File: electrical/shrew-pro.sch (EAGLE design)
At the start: 52 parts, among them IC1 LMR16006YQ3DDCTQ1, U1 ESP32-PICO-D4, U2 SX1280IMLTRT, U3 DRV8244SQRYJRQ1, U4 DRV8244SQRYJRQ1, X1 PIN-1X-BIG, X2 PIN-1X-BIG, X3 PIN-1X-BIG, X4 PIN-1X-BIG, X5 PIN-1X-BIG, X6 PIN-1X-BIG, Y1 52MHz TCXO

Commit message: placed a PCBA order for shrew-lite
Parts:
- C14, C15: value (none) -> 100n
- C16, C18, C19, C20, C21, C22, C23: value (none) -> 10u
- R4: value (none) -> 68K
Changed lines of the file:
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@@
 <part name="X3" library="shrew-core" deviceset="PIN-1X" device="-BIG"/>
 <part name="X4" library="shrew-core" deviceset="PIN-1X" device="-BIG"/>
-<part name="C14" library="shrew-common" deviceset="CAP" device="0402-CAP"/>
-<part name="C15" library="shrew-common" deviceset="CAP" device="0402-CAP"/>
+<part name="C14" library="shrew-common" deviceset="CAP" device="0402-CAP" value="100n"/>
+<part name="C15" library="shrew-common" deviceset="CAP" device="0402-CAP" value="100n"/>
 <part name="X5" library="shrew-core" deviceset="PIN-1X" device="-BIG" value="PIN-1X-BIG"/>
 <part name="P+11" library="shrew-common" deviceset="+24V" device=""/>
 <part name="X6" library="shrew-core" deviceset="PIN-1X" device="-BIG" value="PIN-1X-BIG"/>
 <part name="GND24" library="shrew-common" deviceset="GND" device=""/>
-<part name="C16" library="shrew-common" deviceset="CAP" device="0805"/>
-<part name="C18" library="shrew-common" deviceset="CAP" device="0805"/>
-<part name="C19" library="shrew-common" deviceset="CAP" device="0805"/>
+<part name="C16" library="shrew-common" deviceset="CAP" device="0805" value="10u"/>
+<part name="C18" library="shrew-common" deviceset="CAP" device="0805" value="10u"/>
+<part name="C19" library="shrew-common" deviceset="CAP" device="0805" value="10u"/>
 <part name="P+14" library="shrew-common" deviceset="+24V" device=""/>
 <part name="GND25" library="shrew-common" deviceset="GND" device=""/>
-<part name="C20" library="shrew-common" deviceset="CAP" device="0805"/>
+<part name="C20" library="shrew-common" deviceset="CAP" device="0805" value="10u"/>
 <part name="C25" library="shrew-common" deviceset="CAP" device="0805" value="10u"/>
 <part name="GND23" library="shrew-common" deviceset="GND" device=""/>
-<part name="R4" library="shrew-common" deviceset="RESISTOR" device="0402-REV"/>
+<part name="R4" library="shrew-common" deviceset="RESISTOR" device="0402-REV" value="68K"/>
 <part name="P+10" library="shrew-common" deviceset="+24V" device=""/>
 <part name="U3" library="shrew-core" deviceset="DRV8244SQRYJRQ1" device=""/>
@@
 <part name="GND29" library="shrew-common" deviceset="GND" device=""/>
 <part name="GND30" library="shrew-common" deviceset="GND" device=""/>
-<part name="C21" library="shrew-common" deviceset="CAP" device="0805"/>
-<part name="C22" library="shrew-common" deviceset="CAP" device="0805"/>
-<part name="C23" library="shrew-common" deviceset="CAP" device="0805"/>
+<part name="C21" library="shrew-common" deviceset="CAP" device="0805" value="10u"/>
+<part name="C22" library="shrew-common" deviceset="CAP" device="0805" value="10u"/>
+<part name="C23" library="shrew-common" deviceset="CAP" device="0805" value="10u"/>
 <part name="P+17" library="shrew-common" deviceset="3.3V" device=""/>
 <part name="C24" library="shrew-common" deviceset="CAP" device="0805" value="10u"/>
@@
 <instance part="X6" gate="G$1" x="429.26" y="124.46"/>
 <instance part="GND24" gate="1" x="421.64" y="119.38"/>
-<instance part="C16" gate="G$1" x="421.64" y="86.36"/>
-<instance part="C18" gate="G$1" x="431.8" y="86.36"/>
-<instance part="C19" gate="G$1" x="441.96" y="86.36"/>
+<instance part="C16" gate="G$1" x="421.64" y="86.36" smashed="yes">
+<attribute name="NAME" x="423.164" y="89.281" size="1.778" layer="95"/>
+</instance>
+<instance part="C18" gate="G$1" x="431.8" y="86.36" smashed="yes">
+<attribute name="NAME" x="433.324" y="89.281" size="1.778" layer="95"/>
+</instance>
+<instance part="C19" gate="G$1" x="441.96" y="86.36" smashed="yes">
+<attribute name="NAME" x="443.484" y="89.281" size="1.778" layer="95"/>
+</instance>
 <instance part="P+14" gate="1" x="421.64" y="99.06"/>
 <instance part="GND25" gate="1" x="421.64" y="76.2"/>
-<instance part="C20" gate="G$1" x="452.12" y="86.36"/>
+<instance part="C20" gate="G$1" x="452.12" y="86.36" smashed="yes">
+<attribute name="NAME" x="453.644" y="89.281" size="1.778" layer="95"/>
+</instance>
 <instance part="C25" gate="G$1" x="393.7" y="149.86"/>
 <instance part="GND23" gate="1" x="474.98" y="114.3"/>
@@
 <instance part="GND29" gate="1" x="431.8" y="-43.18"/>
 <instance part="GND30" gate="1" x="431.8" y="15.24"/>
-<instance part="C21" gate="G$1" x="462.28" y="86.36"/>
-<instance part="C22" gate="G$1" x="472.44" y="86.36"/>
-<instance part="C23" gate="G$1" x="482.6" y="86.36"/>
+<instance part="C21" gate="G$1" x="462.28" y="86.36" smashed="yes">
+<attribute name="NAME" x="463.804" y="89.281" size="1.778" layer="95"/>
+</instance>
+<instance part="C22" gate="G$1" x="472.44" y="86.36" smashed="yes">
+<attribute name="NAME" x="473.964" y="89.281" size="1.778" layer="95"/>
+</instance>
+<instance part="C23" gate="G$1" x="482.6" y="86.36" smashed="yes">
+<attribute name="NAME" x="484.124" y="89.281" size="1.778" layer="95"/>
+</instance>
 <instance part="P+17" gate="G$1" x="474.98" y="132.08"/>
 <instance part="C24" gate="G$1" x="510.54" y="91.44"/>

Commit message: wip
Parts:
- added TP1, TP2, TP3: M01-1.0MM-TP, shrew-common:M01-1.0MM-TP
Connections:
- net RADIO-RST: now also TP3.1
- net SIG1: now also TP1.1
- net SIG2: now also TP2.1
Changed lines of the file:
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@@
 <part name="P+8" library="shrew-common" deviceset="+24V" device=""/>
 <part name="C27" library="shrew-common" deviceset="CAP" device="0805" value="10u"/>
+<part name="TP1" library="shrew-common" deviceset="M01" device="-1.0MM-TP" value=""/>
+<part name="TP2" library="shrew-common" deviceset="M01" device="-1.0MM-TP" value=""/>
+<part name="TP3" library="shrew-common" deviceset="M01" device="-1.0MM-TP" value=""/>
 </parts>
 <sheets>
@@
 <instance part="P+8" gate="1" x="322.58" y="172.72"/>
 <instance part="C27" gate="G$1" x="474.98" y="124.46"/>
+<instance part="TP1" gate="G$1" x="386.08" y="-20.32"/>
+<instance part="TP2" gate="G$1" x="386.08" y="-33.02"/>
+<instance part="TP3" gate="G$1" x="386.08" y="-48.26"/>
 </instances>
 <busses>
@@
 <label x="431.8" y="-15.24" size="1.27" layer="95" rot="R180" xref="yes"/>
 </segment>
+<segment>
+<pinref part="TP3" gate="G$1" pin="1"/>
+<wire x1="393.7" y1="-48.26" x2="396.24" y2="-48.26" width="0.1524" layer="91"/>
+<label x="396.24" y="-48.26" size="1.27" layer="95" xref="yes"/>
+</segment>
 </net>
 <net name="RADIO-BUSY" class="0">
@@
 <label x="431.8" y="-25.4" size="1.27" layer="95" rot="R180" xref="yes"/>
 </segment>
+<segment>
+<pinref part="TP2" gate="G$1" pin="1"/>
+<wire x1="393.7" y1="-33.02" x2="396.24" y2="-33.02" width="0.1524" layer="91"/>
+<label x="396.24" y="-33.02" size="1.27" layer="95" xref="yes"/>
+</segment>
 </net>
 <net name="SIG1" class="0">
@@
 <label x="431.8" y="-20.32" size="1.27" layer="95" rot="R180" xref="yes"/>
 </segment>
-</net>
+<segment>
+<pinref part="TP1" gate="G$1" pin="1"/>
+<wire x1="393.7" y1="-20.32" x2="396.24" y2="-20.32" width="0.1524" layer="91"/>
+<label x="396.24" y="-20.32" size="1.27" layer="95" xref="yes"/>
+</segment>
+</net>

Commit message: sorted component ref des
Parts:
- removed FL1: 2450FM07D0034T, shrew-core:2450FM07D0034T
- added Y2: 52MHz TCXO, shrew-common:OSCILLATOR-TG2016SMN
- C1: value 1n -> 100n
- C10, C5, C6, C7, C8, C9: value 100n -> 10u; device shrew-common:CAP0402-REV -> shrew-common:CAP0805
- C11: value 10uF 25V -> 10u
- C12: value DNP -> 100n; device shrew-common:CAP0402-CAP -> shrew-common:CAP0402-REV
- C13: value 470n -> 100n
- C14: device shrew-common:CAP0402-CAP -> shrew-common:CAP0402-REV
- C15: value 100n -> 10uF 25V; device shrew-common:CAP0402-CAP -> shrew-common:CAP0805
- C16, C18, C25: value 10u -> 470n; device shrew-common:CAP0805 -> shrew-common:CAP0402-REV
- C17: value 470n -> DNP; device shrew-common:CAP0402-REV -> shrew-common:CAP0402-CAP
- C19, C20: value 10u -> 10n; device shrew-common:CAP0805 -> shrew-common:CAP0402-REV
- C2: value 470n -> 10u; device shrew-common:CAP0402-REV -> shrew-common:CAP0805
- C21: value 10u -> 1n; device shrew-common:CAP0805 -> shrew-common:CAP0402-REV
- C22, C23, C24: value 10u -> 100n; device shrew-common:CAP0805 -> shrew-common:CAP0402-REV
- C26: device shrew-common:CAP0402-REV -> shrew-common:CAP0402-CAP
- C27: value 10u -> 100n; device shrew-common:CAP0805 -> shrew-common:CAP0402-CAP
- C3, C4: value 10n -> 10u; device shrew-common:CAP0402-REV -> shrew-common:CAP0805
- D1: value 3V6 -> (none); device shrew-common:DIODE-ZENER-BZT52 -> shrew-common:DIODESOD
- D2: value (none) -> 3V6; device shrew-common:DIODESOD -> shrew-common:DIODE-ZENER-BZT52
- L1: value 15u -> 6u8
- L2: value 6u8 -> 15u
- R2: value 10K -> 68K
- R4: value 68K -> 10K
- U3, U4: value DRV8244SQRYJRQ1 -> DRV8244HQRYJRQ1
- Y1: value 52MHz TCXO -> 2450FM07D0034T; device shrew-common:OSCILLATOR-TG2016SMN -> shrew-core:2450FM07D0034T
- renumbered EDGE1 to JP1
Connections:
- net +24V: now also C10.1, C11.1, C3.1, C5.1, C6.1, C7.1, C8.1, C9.1, R2.2, X1.P$1; no longer C16.1, C18.1, C19.1, C20.1, C21.1, C22.1, C23.1, C24.1, R4.2, X5.P$1
- net 3.3V: now also C12.1, C13.1, C14.1, C15.1, C2.1, C22.2, C23.2, C24.2, C4.1, L1.2, Y2.VCC; no longer C10.1, C11.1, C25.1, C27.1, C5.2, C6.2, C7.2, C8.1, C9.1, L2.2, Y1.VCC
- net BATT-ADC: now also C18.1, D2.C, R4.2; no longer C17.1, D1.C, R2.2
- net ESP-BOOT: now also C17.2; no longer C12.2
- net ESP-EN: now also C16.2; no longer C13.2
- net GND: now also C12.2, C13.2, C14.2, C15.2, C16.1, C17.1, C19.1, C2.2, C20.1, C22.1, C23.1, C24.1, C25.1, C3.2, C4.2, C5.2, C6.2, C7.2, R4.1, X2.P$1, Y2.GND; no longer C12.1, C13.1, C16.2, C17.2, C19.2, C2.1, C20.2, C21.2, C22.2, C23.2, C24.2, C25.2, C27.2, C3.1, C4.1, C5.1, C6.1, C7.1, R2.1, X6.P$1, Y1.GND
- net MOTOR1: now also C26.1, X3.P$1; no longer C14.1, X2.P$1
- net MOTOR2: now also C26.2, X4.P$1; no longer C14.2, X1.P$1
- net MOTOR3: now also C27.1, X5.P$1; no longer C15.1, X4.P$1
- net MOTOR4: now also C27.2, X6.P$1; no longer C15.2, X3.P$1
- net N$10: now also C1.1, D1.C, L1.1; no longer C26.1, D2.C, L2.1
- net N$11: now also C20.2; no longer C3.2
- net N$2: now also C21.1, Y2.OUT; no longer C1.1, Y1.OUT
- net N$3: now also C21.2; no longer C1.2
- net N$4: now also C1.2; no longer C26.2
- net N$6: now also Y1.IN; no longer FL1.IN
- net N$7: now also Y1.OUT; no longer FL1.OUT
- net N$9: now also L2.2; no longer L1.2
- net RADIO-VDD: now also C19.2, C25.2, L2.1; no longer C2.2, C4.2, L1.1
- net V-ADC: now also R2.1; no longer R4.1
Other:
- moved on the sheet: ANT2, C1, C10, C11, C12, C13, C14, C15, C16, C17, C18, C19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

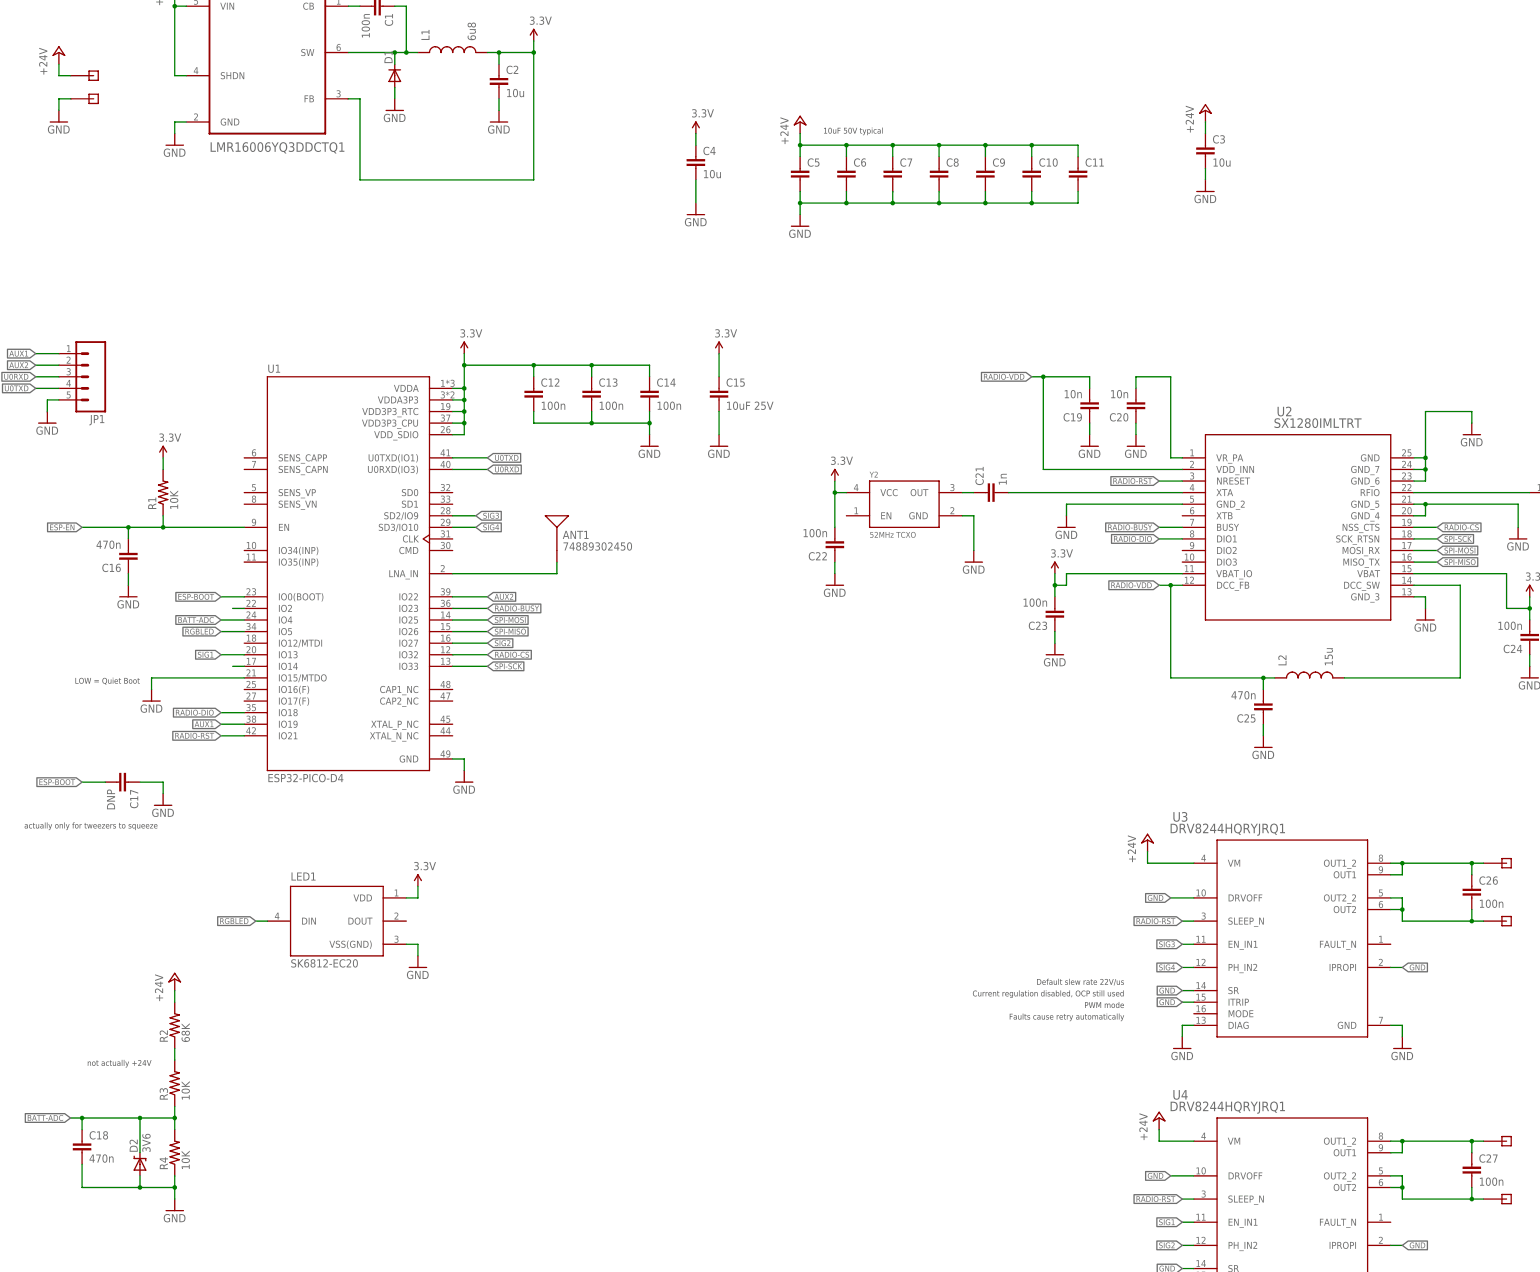
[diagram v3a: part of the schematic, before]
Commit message: shrew-pro with additional capacitors
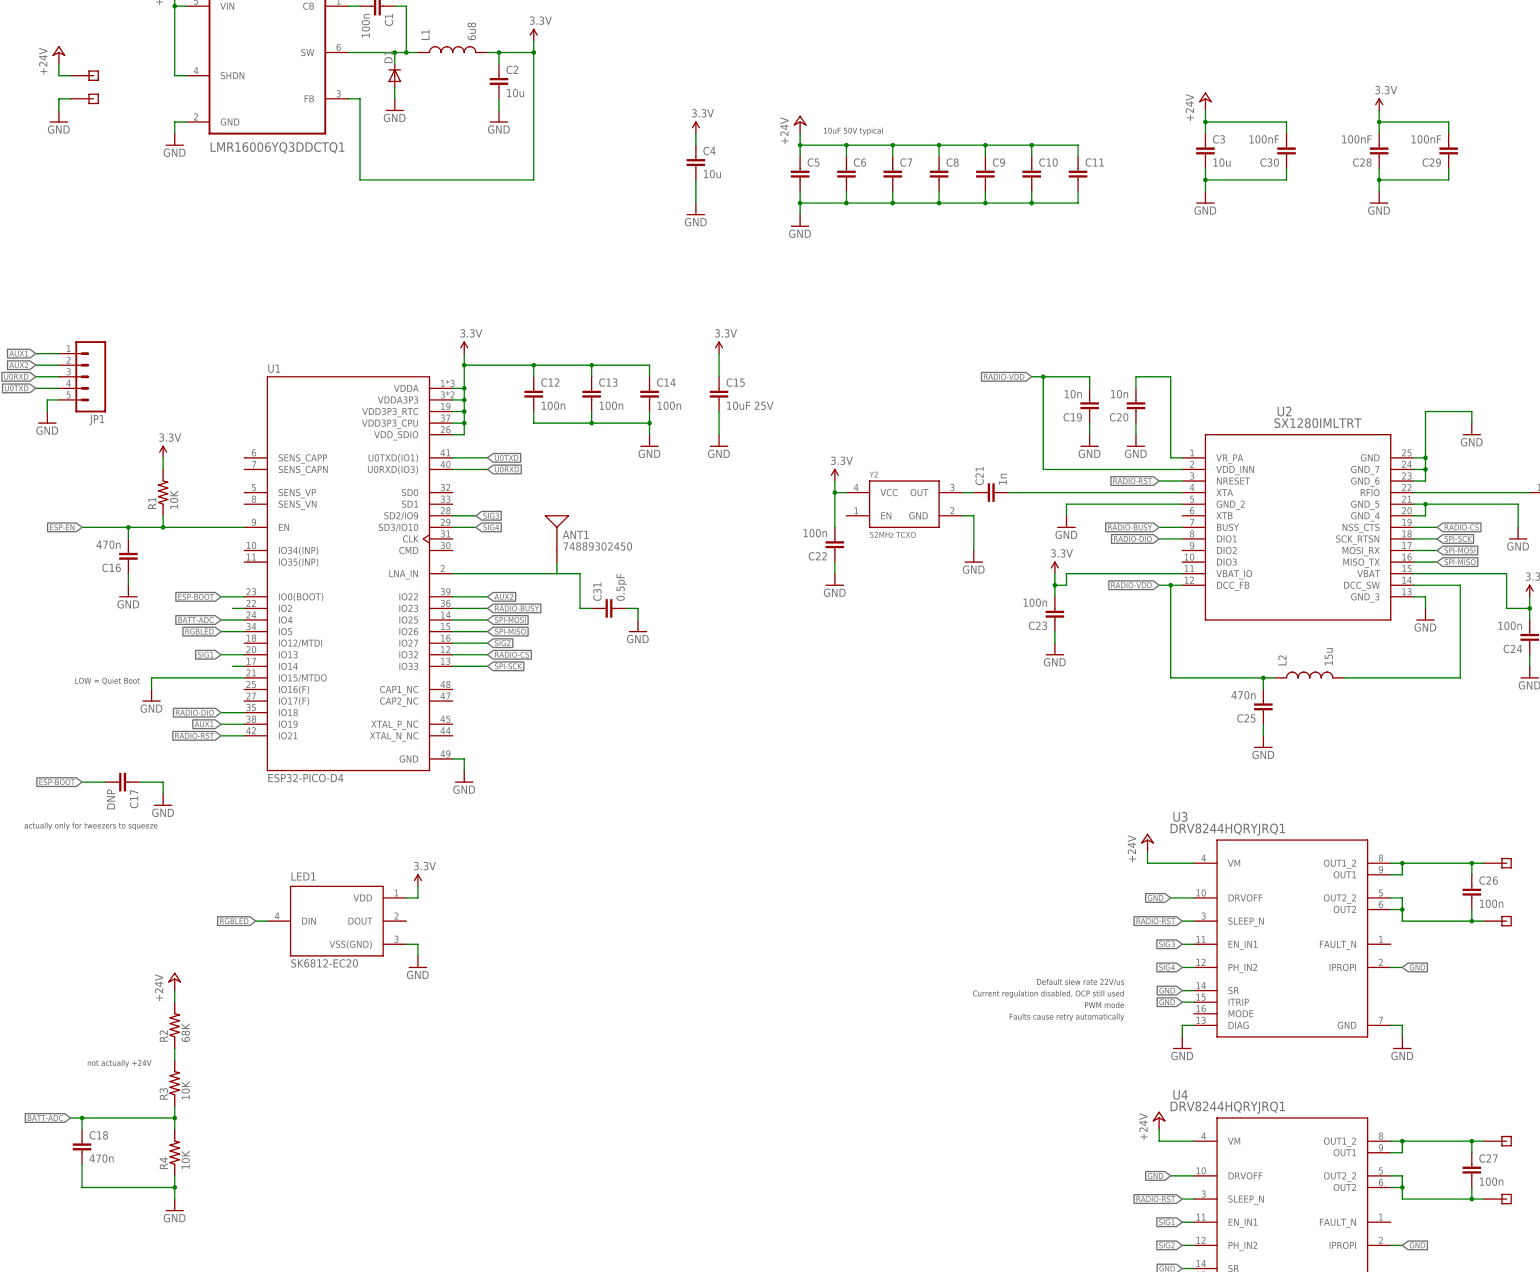
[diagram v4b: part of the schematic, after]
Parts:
- removed D2: 3V6, shrew-common:DIODE-ZENER-BZT52
- added C28, C29: 100nF, shrew-common:CAP0402-CAP
- added C30: 100nF, shrew-common:CAP0402-REV
- added C31: 0.5pF, shrew-common:CAP0402-CAP
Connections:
- net +24V: now also C30.2
- net 3.3V: now also C28.2, C29.2
- net BATT-ADC: no longer D2.C
- net GND: now also C28.1, C29.1, C30.1, C31.2; no longer D2.A
- net N$1: now also C31.1
